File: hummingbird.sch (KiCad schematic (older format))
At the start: 35 parts

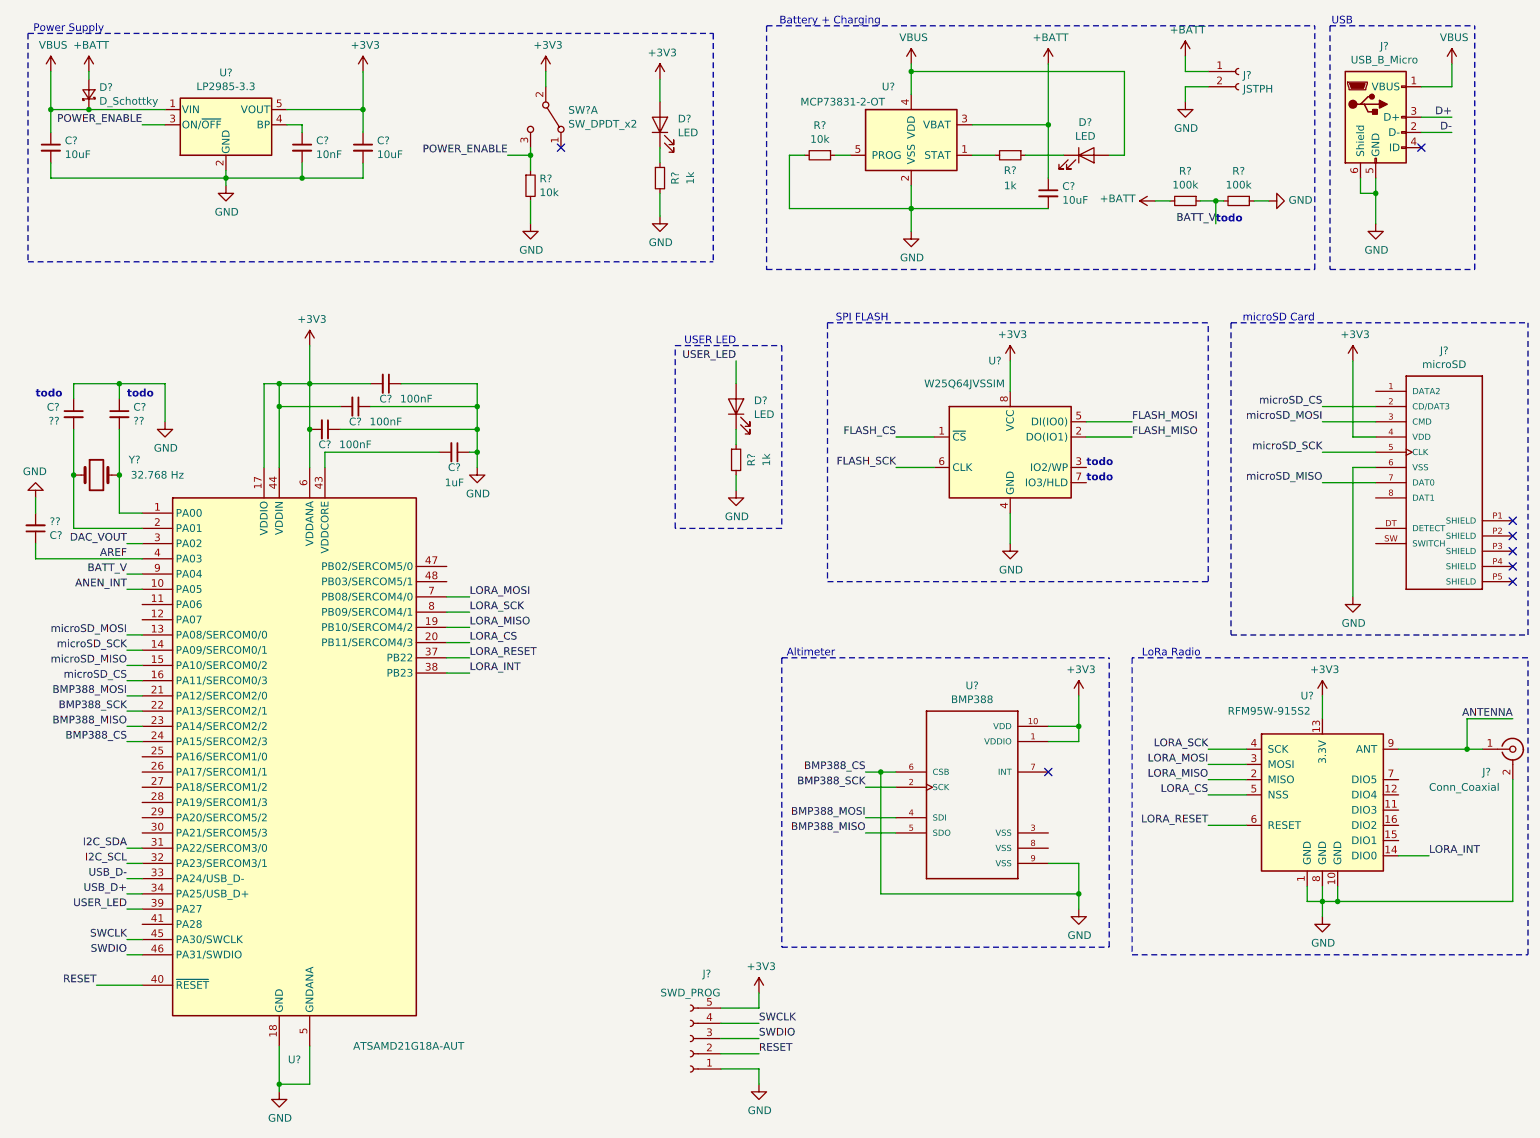
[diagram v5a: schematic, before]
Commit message: finish spi wiring, add connectors
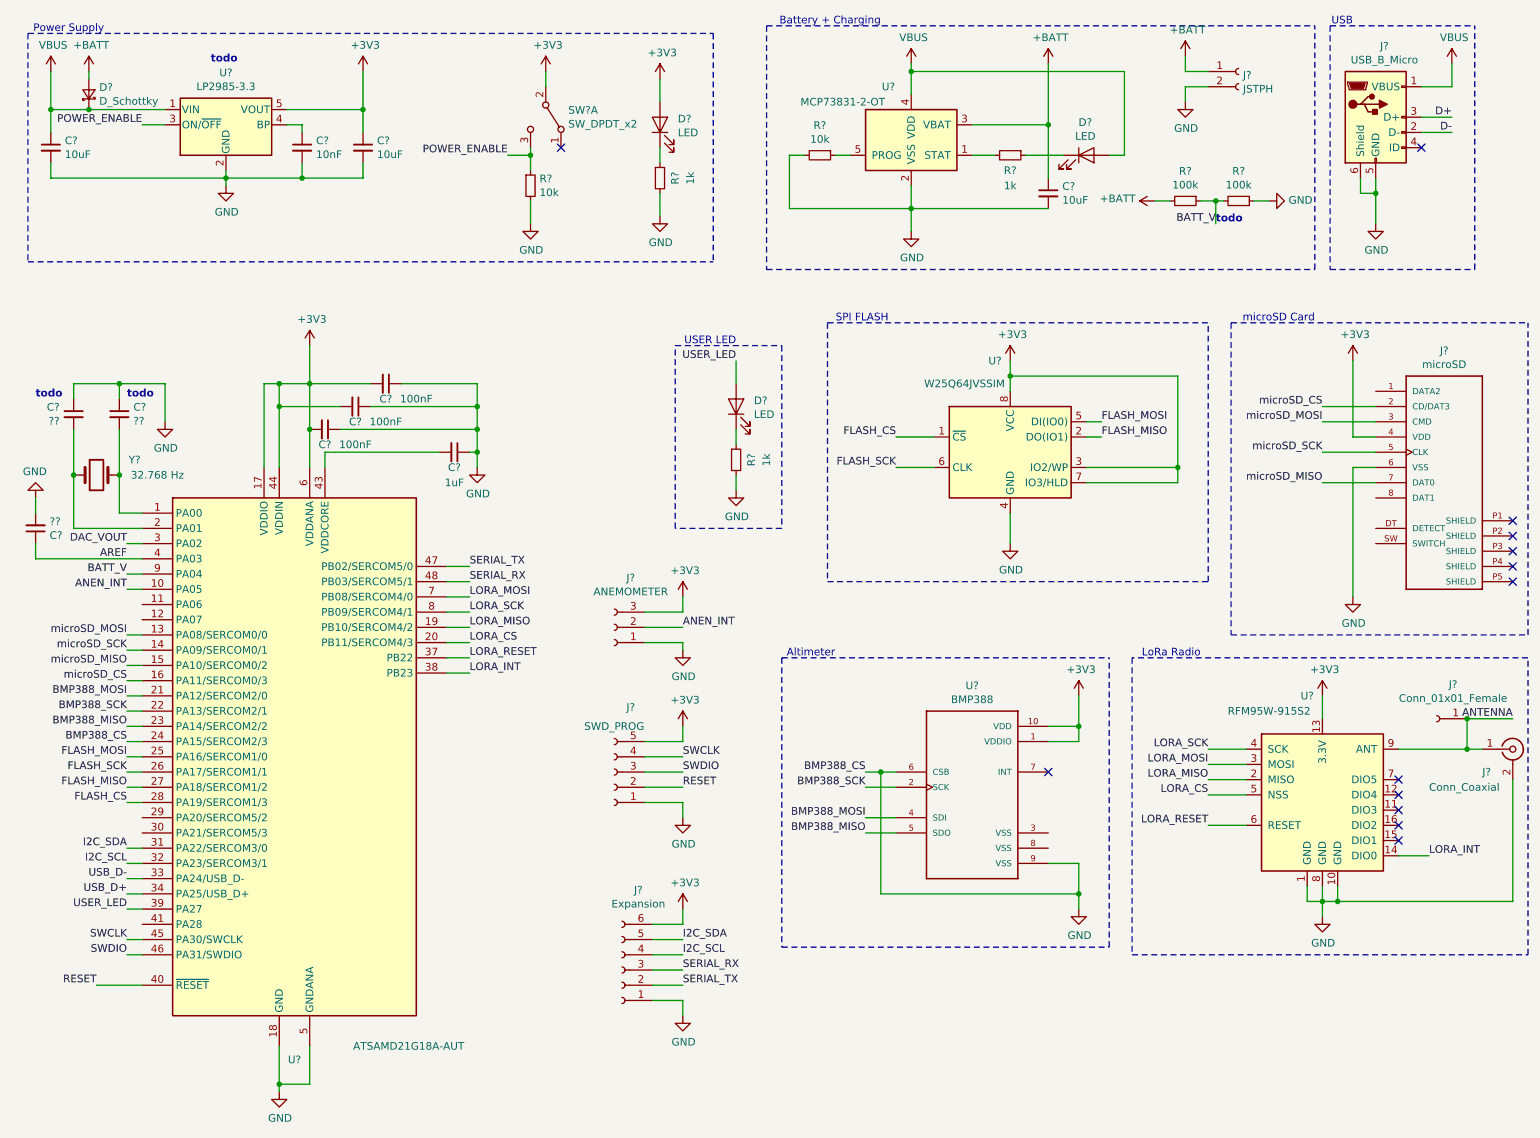
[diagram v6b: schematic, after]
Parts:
- added J?: ANEMOMETER, symbol Connector:Conn_01x03_Female
- added J?: Expansion, symbol Connector:Conn_01x06_Female
- added J?: Conn_01x01_Female, symbol Connector:Conn_01x01_Female
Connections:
- net +3V3: now also U?.3 (IO2/WP), U?.7 (IO3/HLD), J?.3 (Pin_3), J?.6 (Pin_6)
- net ANEN_INT: now also J?.2 (Pin_2)
- net ANTENNA: now also J?.1 (Pin_1)
- net FLASH_CS: now also U?.28 (PA19/SERCOM1/3)
- net FLASH_MISO: now also U?.27 (PA18/SERCOM1/2)
- net FLASH_MOSI: now also U?.25 (PA16/SERCOM1/0)
- net FLASH_SCK: now also U?.26 (PA17/SERCOM1/1)
- net GND: now also J?.1 (Pin_1), J?.1 (Pin_1)
- net I2C_SCL: now also J?.4 (Pin_4)
- net I2C_SDA: now also J?.5 (Pin_5)
- net SERIAL_TX: now reaches U?.47 (PB02/SERCOM5/0)
- net SERIAL_TX: now also J?.2 (Pin_2)
- net SERIAL_RX: now reaches U?.48 (PB03/SERCOM5/1)
- net SERIAL_RX: now also J?.3 (Pin_3)
- no-connect marks 8 -> 13
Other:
- moved on the sheet: J?
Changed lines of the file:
@@
 $EndComp
 Wire Wire Line
-	7050 2800 7050 3000
+	7050 2800 7050 2900
 Wire Wire Line
 	6550 3300 6300 3300
@@
 Text Label 6300 3500 2    50   ~ 0
 FLASH_SCK
-Wire Wire Line
-	7550 3200 7850 3200
-Wire Wire Line
-	7550 3300 7850 3300
-Text Label 7850 3200 0    50   ~ 0
+Text Label 7650 3200 0    50   ~ 0
 FLASH_MOSI
-Text Label 7850 3300 0    50   ~ 0
+Text Label 7650 3300 0    50   ~ 0
 FLASH_MISO
 Wire Wire Line
@@
 L Connector:Conn_01x05_Female J?
 U 1 1 5D165227
-P 4950 7250
-F 0 "J?" H 4842 6825 50  0000 C CNN
-F 1 "SWD_PROG" H 4950 6950 50  0000 C CNN
-F 2 "" H 4950 7250 50  0001 C CNN
-F 3 "~" H 4950 7250 50  0001 C CNN
-	1    4950 7250
+P 4450 5500
+F 0 "J?" H 4342 5075 50  0000 C CNN
+F 1 "SWD_PROG" H 4450 5200 50  0000 C CNN
+F 2 "" H 4450 5500 50  0001 C CNN
+F 3 "~" H 4450 5500 50  0001 C CNN
+	1    4450 5500
 	-1   0    0    1
 $EndComp
 Wire Wire Line
-	5150 7450 5400 7450
+	4650 5700 4900 5700
 $Comp
 L power:GND #PWR?
 U 1 1 5D16B7BA
-P 5400 7550
-F 0 "#PWR?" H 5400 7300 50  0001 C CNN
-F 1 "GND" H 5405 7377 50  0000 C CNN
-F 2 "" H 5400 7550 50  0001 C CNN
-F 3 "" H 5400 7550 50  0001 C CNN
-	1    5400 7550
-	1    0    0    -1
-$EndComp
-Wire Wire Line
-	5400 7450 5400 7550
-Wire Wire Line
-	5150 7050 5400 7050
-Wire Wire Line
-	5400 7050 5400 6950
+P 4900 5800
+F 0 "#PWR?" H 4900 5550 50  0001 C CNN
+F 1 "GND" H 4905 5627 50  0000 C CNN
+F 2 "" H 4900 5800 50  0001 C CNN
+F 3 "" H 4900 5800 50  0001 C CNN
+	1    4900 5800
+	1    0    0    -1
+$EndComp
+Wire Wire Line
+	4900 5700 4900 5800
+Wire Wire Line
+	4650 5300 4900 5300
+Wire Wire Line
+	4900 5300 4900 5200
 $Comp
 L power:+3V3 #PWR?
 U 1 1 5D1782FB
-P 5400 6950
-F 0 "#PWR?" H 5400 6800 50  0001 C CNN
-F 1 "+3V3" H 5415 7123 50  0000 C CNN
-F 2 "" H 5400 6950 50  0001 C CNN
-F 3 "" H 5400 6950 50  0001 C CNN
-	1    5400 6950
-	1    0    0    -1
-$EndComp
-Wire Wire Line
-	5150 7150 5400 7150
-Wire Wire Line
-	5150 7250 5400 7250
-Wire Wire Line
-	5150 7350 5400 7350
-Text Label 5400 7150 0    50   ~ 0
+P 4900 5200
+F 0 "#PWR?" H 4900 5050 50  0001 C CNN
+F 1 "+3V3" H 4915 5373 50  0000 C CNN
+F 2 "" H 4900 5200 50  0001 C CNN
+F 3 "" H 4900 5200 50  0001 C CNN
+	1    4900 5200
+	1    0    0    -1
+$EndComp
+Wire Wire Line
+	4650 5400 4900 5400
+Wire Wire Line
+	4650 5500 4900 5500
+Wire Wire Line
+	4650 5600 4900 5600
+Text Label 4900 5400 0    50   ~ 0
 SWCLK
-Text Label 5400 7250 0    50   ~ 0
+Text Label 4900 5500 0    50   ~ 0
 SWDIO
-Text Label 5400 7350 0    50   ~ 0
+Text Label 4900 5600 0    50   ~ 0
 RESET
-Text Notes 7550 3500 0    50   ~ 10
-todo
-Text Notes 7550 3600 0    50   ~ 10
-todo
 Text Notes 8400 1900 0    50   ~ 10
 todo
@@
 Wire Wire Line
 	3350 4850 3500 4850
+Wire Wire Line
+	7550 3200 7650 3200
+Wire Wire Line
+	7550 3300 7650 3300
+Wire Wire Line
+	7550 3500 8150 3500
+Wire Wire Line
+	8150 3500 8150 2900
+Wire Wire Line
+	8150 2900 7050 2900
+Connection ~ 7050 2900
+Wire Wire Line
+	7050 2900 7050 3000
+Wire Wire Line
+	7550 3600 8150 3600
+Wire Wire Line
+	8150 3600 8150 3500
+Connection ~ 8150 3500
+NoConn ~ 9600 5550
+NoConn ~ 9600 5650
+NoConn ~ 9600 5750
+NoConn ~ 9600 5850
+NoConn ~ 9600 5950
+$Comp
+L Connector:Conn_01x03_Female J?
+U 1 1 5D1467C0
+P 4450 4550
+F 0 "J?" H 4342 4225 50  0000 C CNN
+F 1 "ANEMOMETER" H 4342 4316 50  0000 C CNN
+F 2 "" H 4450 4550 50  0001 C CNN
+F 3 "~" H 4450 4550 50  0001 C CNN
+	1    4450 4550
+	-1   0    0    1
+$EndComp
+$Comp
+L Connector:Conn_01x06_Female J?
+U 1 1 5D154284
+P 4500 6800
+F 0 "J?" H 4392 6275 50  0000 C CNN
+F 1 "Expansion" H 4392 6366 50  0000 C CNN
+F 2 "" H 4500 6800 50  0001 C CNN
+F 3 "~" H 4500 6800 50  0001 C CNN
+	1    4500 6800
+	-1   0    0    1
+$EndComp
+$Comp
+L power:+3V3 #PWR?
+U 1 1 5D154BAD
+P 4900 4350
+F 0 "#PWR?" H 4900 4200 50  0001 C CNN
+F 1 "+3V3" H 4915 4523 50  0000 C CNN
+F 2 "" H 4900 4350 50  0001 C CNN
+F 3 "" H 4900 4350 50  0001 C CNN
+	1    4900 4350
+	1    0    0    -1
+$EndComp
+Wire Wire Line
+	4900 4450 4900 4350
+$Comp
+L power:GND #PWR?
+U 1 1 5D1699C3
+P 4900 4700
+F 0 "#PWR?" H 4900 4450 50  0001 C CNN
+F 1 "GND" H 4905 4527 50  0000 C CNN
+F 2 "" H 4900 4700 50  0001 C CNN
+F 3 "" H 4900 4700 50  0001 C CNN
+	1    4900 4700
+	1    0    0    -1
+$EndComp
+Wire Wire Line
+	4900 4650 4900 4700
+Text Label 4900 4550 0    50   ~ 0
+ANEN_INT
+Wire Wire Line
+	4650 4450 4900 4450
+Wire Wire Line
+	4650 4550 4900 4550
+Wire Wire Line
+	4650 4650 4900 4650
+$Comp
+L power:GND #PWR?
+U 1 1 5D1A8337
+P 4900 7100
+F 0 "#PWR?" H 4900 6850 50  0001 C CNN
+F 1 "GND" H 4905 6927 50  0000 C CNN
+F 2 "" H 4900 7100 50  0001 C CNN
+F 3 "" H 4900 7100 50  0001 C CNN
+	1    4900 7100
+	1    0    0    -1
+$EndComp
+Wire Wire Line
+	4700 7000 4900 7000
+Wire Wire Line
+	4900 7000 4900 7100
+$Comp
+L power:+3V3 #PWR?
+U 1 1 5D1B30B8
+P 4900 6400
+F 0 "#PWR?" H 4900 6250 50  0001 C CNN
+F 1 "+3V3" H 4915 6573 50  0000 C CNN
+F 2 "" H 4900 6400 50  0001 C CNN
+F 3 "" H 4900 6400 50  0001 C CNN
+	1    4900 6400
+	1    0    0    -1
+$EndComp
+Wire Wire Line
+	4700 6500 4900 6500
+Wire Wire Line
+	4900 6500 4900 6400
+Wire Wire Line
+	4700 6600 4900 6600
+Text Label 4900 6600 0    50   ~ 0
+I2C_SDA
+Wire Wire Line
+	4700 6700 4900 6700
+Text Label 4900 6700 0    50   ~ 0
+I2C_SCL
+Wire Wire Line
+	4700 6800 4900 6800
+Text Label 4900 6800 0    50   ~ 0
+SERIAL_RX
+Wire Wire Line
+	4700 6900 4900 6900
+Text Label 4900 6900 0    50   ~ 0
+SERIAL_TX
+Text Label 1250 5700 2    50   ~ 0
+FLASH_CS
+Text Label 1250 5500 2    50   ~ 0
+FLASH_SCK
+Text Label 1250 5400 2    50   ~ 0
+FLASH_MOSI
+Text Label 1250 5600 2    50   ~ 0
+FLASH_MISO
+Wire Wire Line
+	1250 5400 1350 5400
+Wire Wire Line
+	1250 5500 1350 5500
+Wire Wire Line
+	1250 5600 1350 5600
+Wire Wire Line
+	1250 5700 1350 5700
+Text Label 3500 4150 0    50   ~ 0
+SERIAL_TX
+Text Label 3500 4250 0    50   ~ 0
+SERIAL_RX
+Wire Wire Line
+	3350 4150 3500 4150
+Wire Wire Line
+	3350 4250 3500 4250
+$Comp
+L Connector:Conn_01x01_Female J?
+U 1 1 5D2324C9
+P 9850 5150
+F 0 "J?" H 9742 4925 50  0000 C CNN
+F 1 "Conn_01x01_Female" H 9742 5016 50  0000 C CNN
+F 2 "" H 9850 5150 50  0001 C CNN
+F 3 "~" H 9850 5150 50  0001 C CNN
+	1    9850 5150
+	-1   0    0    1
+$EndComp
+Connection ~ 10050 5150
+Text Notes 1800 850  0    50   ~ 10
+todo
 $EndSCHEMATC

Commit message: new voltage regulator, add pullups on CS, fix BMP388 CS
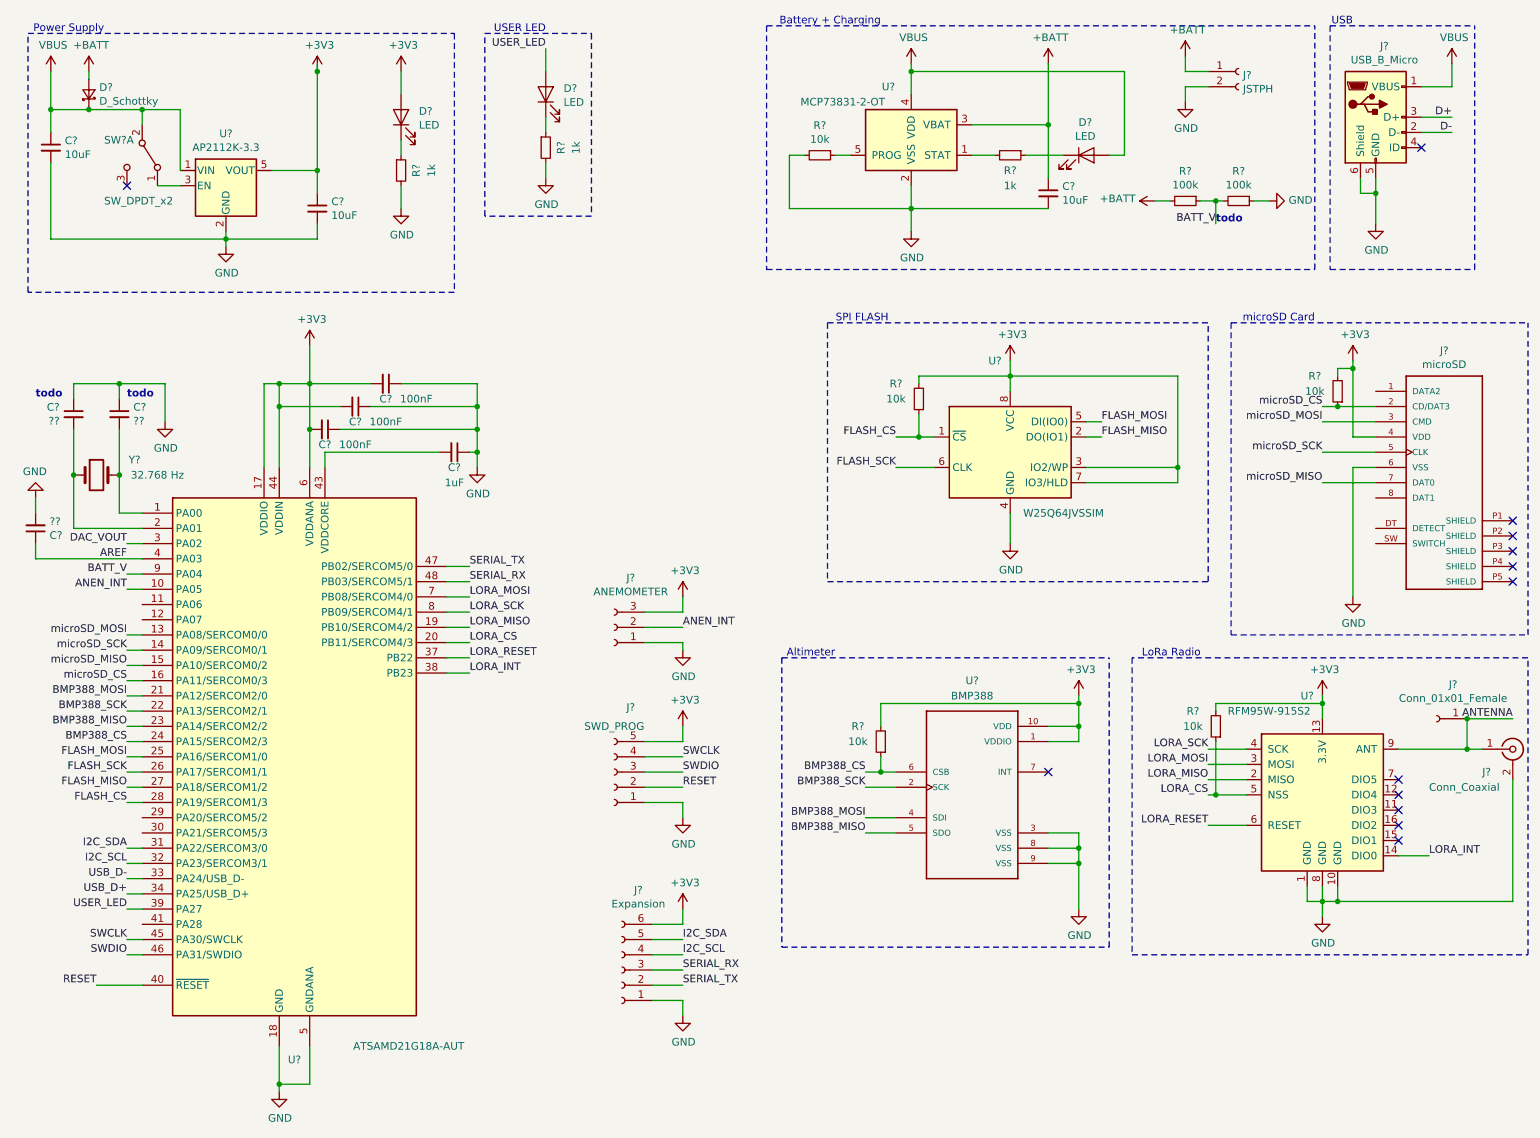
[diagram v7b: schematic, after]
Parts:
- removed C?: 10nF, symbol Device:C_Small
- removed R?: 10k, symbol Device:R_Small
- removed U?: LP2985-3.3, Package_TO_SOT_SMD:SOT-23-5, symbol symbols:LP2985-3.3
- added R? (x4): 10k, symbol Device:R_Small
- added U?: AP2112K-3.3, Package_TO_SOT_SMD:SOT-23-5, symbol Regulator_Linear:AP2112K-3.3
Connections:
- net +3V3: now also R?.2, R?.2, R?.2, R?.2, U?.5 (VOUT); no longer SW?.2 (B)
- net FLASH_CS: now also R?.1
- net GND: now also U?.3 (VSS), U?.8 (VSS), U?.2 (GND); no longer U?.24 (PA15/SERCOM2/3), U?.6 (CSB)
- net LORA_CS: now also R?.1
- net VBUS: now also SW?.2 (B), U?.1 (VIN)
- net microSD_CS: now also R?.1
- net at SW?.1 (A): now also U?.3 (EN)
- net POWER_ENABLE: no longer names the net of SW?.3 (C)
- new net BMP388_CS: R?.1, U?.24 (PA15/SERCOM2/3), U?.6 (CSB)
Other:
- moved on the sheet: C?, D?, R?, SW?A

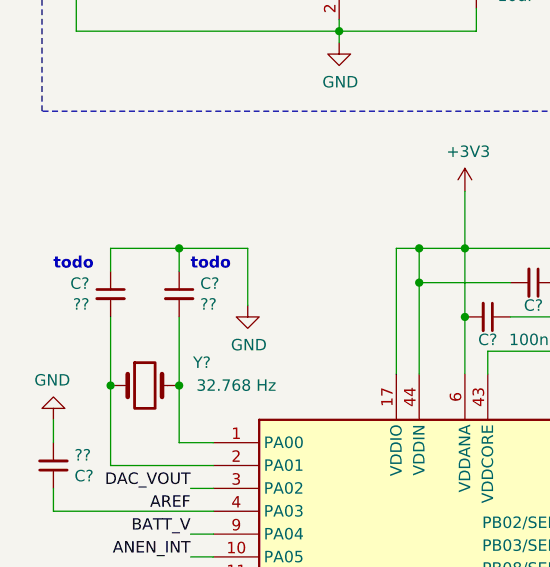
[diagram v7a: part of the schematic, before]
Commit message: add crystal and capacitors
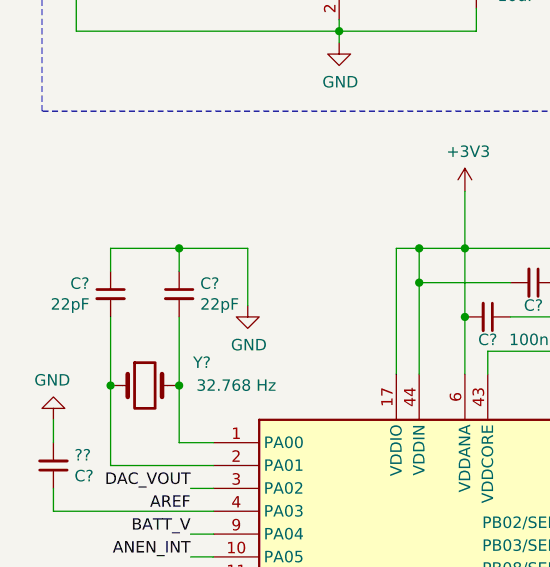
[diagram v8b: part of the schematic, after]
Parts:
- C? (x2): value ?? -> 22pF
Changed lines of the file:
@@
 F 1 "32.768 Hz" H 1450 3550 50  0000 C CNN
 F 2 "" H 1050 3550 50  0001 C CNN
-F 3 "~" H 1050 3550 50  0001 C CNN
+F 3 "https://abracon.com/Resonators/ABS07.pdf" H 1050 3550 50  0001 C CNN
 	1    1050 3550
 	1    0    0    -1
@@
 P 900 3150
 F 0 "C?" H 992 3196 50  0000 L CNN
-F 1 "??" H 992 3105 50  0000 L CNN
+F 1 "22pF" H 992 3105 50  0000 L CNN
 F 2 "" H 900 3150 50  0001 C CNN
 F 3 "~" H 900 3150 50  0001 C CNN
@@
 P 1200 3150
 F 0 "C?" H 1292 3196 50  0000 L CNN
-F 1 "??" H 1292 3105 50  0000 L CNN
+F 1 "22pF" H 1292 3105 50  0000 L CNN
 F 2 "" H 1200 3150 50  0001 C CNN
 F 3 "~" H 1200 3150 50  0001 C CNN
@@
 Text Notes 8400 1900 0    50   ~ 10
 todo
-Text Notes 650  3050 0    50   ~ 10
-todo
-Text Notes 1250 3050 0    50   ~ 10
-todo
 Text Label 1250 6400 2    50   ~ 0
